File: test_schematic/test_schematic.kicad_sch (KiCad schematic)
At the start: 0 parts

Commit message: Put random components
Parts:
- added C1: C, symbol Device:C
- added R1: R, symbol Device:R
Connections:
- new net: C1.2, R1.1
- new net GND: R1.2

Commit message: Test Push
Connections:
- net GND is gone; now on net +3.3V: R1.2
- net +3.3V: now also C1.1, C1.2, R1.1
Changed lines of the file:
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@@
 	(paper "A4")
+	(junction
+		(at 147.32 97.79)
+		(diameter 0)
+		(color 0 0 0 0)
+	)
+	(junction
+		(at 147.32 93.98)
+		(diameter 0)
+		(color 0 0 0 0)
+	)
 	(junction
 		(at 147.32 100.33)
 		(diameter 0)
 		(color 0 0 0 0)
+	)
+	(junction
+		(at 165.1 86.36)
+		(diameter 0)
+		(color 0 0 0 0)
+	)
+	(junction
+		(at 165.1 88.9)
+		(diameter 0)
+		(color 0 0 0 0)
+	)
+	(wire
+		(pts
+			(xy 147.32 97.79) (xy 138.43 97.79)
+		)
+		(stroke
+			(width 0)
+			(type default)
+		)
 	)
 	(wire
@@
 	(wire
 		(pts
-			(xy 147.32 86.36) (xy 147.32 87.63)
+			(xy 168.91 88.9) (xy 165.1 88.9)
+		)
+		(stroke
+			(width 0)
+			(type default)
+		)
+	)
+	(wire
+		(pts
+			(xy 147.32 86.36) (xy 147.32 93.98)
+		)
+		(stroke
+			(width 0)
+			(type default)
+		)
+	)
+	(wire
+		(pts
+			(xy 165.1 88.9) (xy 165.1 90.17)
 		)
 		(stroke
@@
 		(pts
 			(xy 165.1 97.79) (xy 165.1 100.33)
+		)
+		(stroke
+			(width 0)
+			(type default)
+		)
+	)
+	(wire
+		(pts
+			(xy 165.1 86.36) (xy 167.64 86.36)
+		)
+		(stroke
+			(width 0)
+			(type default)
+		)
+	)
+	(wire
+		(pts
+			(xy 144.78 87.63) (xy 144.78 93.98)
+		)
+		(stroke
+			(width 0)
+			(type default)
+		)
+	)
+	(wire
+		(pts
+			(xy 147.32 93.98) (xy 147.32 97.79)
 		)
 		(stroke
@@
 	(wire
 		(pts
-			(xy 165.1 86.36) (xy 165.1 90.17)
+			(xy 165.1 86.36) (xy 165.1 88.9)
 		)
 		(stroke
+			(width 0)
+			(type default)
+		)
+	)
+	(wire
+		(pts
+			(xy 167.64 83.82) (xy 167.64 86.36)
+		)
+		(stroke
+			(width 0)
+			(type default)
+		)
+	)
+	(wire
+		(pts
+			(xy 168.91 83.82) (xy 168.91 88.9)
+		)
+		(stroke
+			(width 0)
+			(type default)
+		)
+	)
+	(wire
+		(pts
+			(xy 144.78 93.98) (xy 147.32 93.98)
+		)
+		(stroke

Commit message: Pushing my Changes
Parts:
- added D1: 1N62xxA, Diode_THT:D_DO-201AE_P15.24mm_Horizontal, symbol Diode:1N62xxA
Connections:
- net +3.3V: now also D1.1 (A1), D1.2 (A2)
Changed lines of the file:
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@@
 	(paper "A4")
+	(junction
+		(at 151.13 100.33)
+		(diameter 0)
+		(color 0 0 0 0)
+	)
 	(junction
 		(at 147.32 97.79)
@@
 	)
 	(junction
+		(at 161.29 100.33)
+		(diameter 0)
+		(color 0 0 0 0)
+	)
+	(junction
 		(at 165.1 86.36)
 		(diameter 0)
@@
 	(wire
 		(pts
+			(xy 151.13 95.25) (xy 151.13 100.33)
+		)
+		(stroke
+			(width 0)
+			(type default)
+		)
+	)
+	(wire
+		(pts
 			(xy 158.75 86.36) (xy 165.1 86.36)
 		)
@@
 	(wire
 		(pts
+			(xy 161.29 95.25) (xy 161.29 100.33)
+		)
+		(stroke
+			(width 0)
+			(type default)
+		)
+	)
+	(wire
+		(pts
 			(xy 147.32 86.36) (xy 147.32 93.98)
 		)
@@
 	(wire
 		(pts
-			(xy 147.32 100.33) (xy 165.1 100.33)
+			(xy 147.32 100.33) (xy 151.13 100.33)
+		)
+		(stroke
+			(width 0)
+			(type default)
+		)
+	)
+	(wire
+		(pts
+			(xy 158.75 95.25) (xy 161.29 95.25)
+		)
+		(stroke
+			(width 0)
+			(type default)
+		)
+	)
+	(wire
+		(pts
+			(xy 161.29 100.33) (xy 165.1 100.33)
 		)
 		(stroke
@@
 		(pts
 			(xy 144.78 93.98) (xy 147.32 93.98)
+		)
+		(stroke
+			(width 0)
+			(type default)
+		)
+	)
+	(wire
+		(pts
+			(xy 151.13 100.33) (xy 161.29 100.33)
 		)
 		(stroke
@@
 					(unit 1)
 				)
+			)
+		)
+	)
+	(symbol
+		(lib_id "Diode:1N62xxA")
+		(at 154.94 95.25 0)
+		(unit 1)
+		(exclude_from_sim no)
+		(in_bom yes)
+		(on_board yes)
+		(dnp no)
+		(fields_autoplaced yes)
+		(property "Reference" "D1"
+			(at 154.94 88.9 0)
+			(effects
+				(font
+					(size 1.27 1.27)
+				)
+			)
+		)
+		(property "Value" "1N62xxA"
+			(at 154.94 91.44 0)
+			(effects
+				(font
+					(size 1.27 1.27)
+				)
+			)
+		)
+		(property "Footprint" "Diode_THT:D_DO-201AE_P15.24mm_Horizontal"
+			(at 154.94 100.33 0)
+			(effects
+				(font
+					(size 1.27 1.27)
+				)
+				(hide yes)
+			)
+		)
+		(property "Datasheet" "https://www.vishay.com/docs/88301/15ke.pdf"
+			(at 153.67 95.25 0)
+			(effects
+				(font
+					(size 1.27 1.27)
+				)
+				(hide yes)
+			)
+		)
+		(property "Description" "1500W unidirectional TRANSZORB® Transient Voltage Suppressor, DO-201AE"
+			(at 154.94 95.25 0)
+			(effects
+				(font
+					(size 1.27 1.27)
+				)
+				(hide yes)
+			)
+		)
+		(pin "1"
+		)
+		(pin "2"
+		)
+		(instances
+			(project ""
+				(path "/34cad894-6d1f-473e-a83f-d88de5da818d"
+					(reference "D1")
+					(unit 1)
+				)

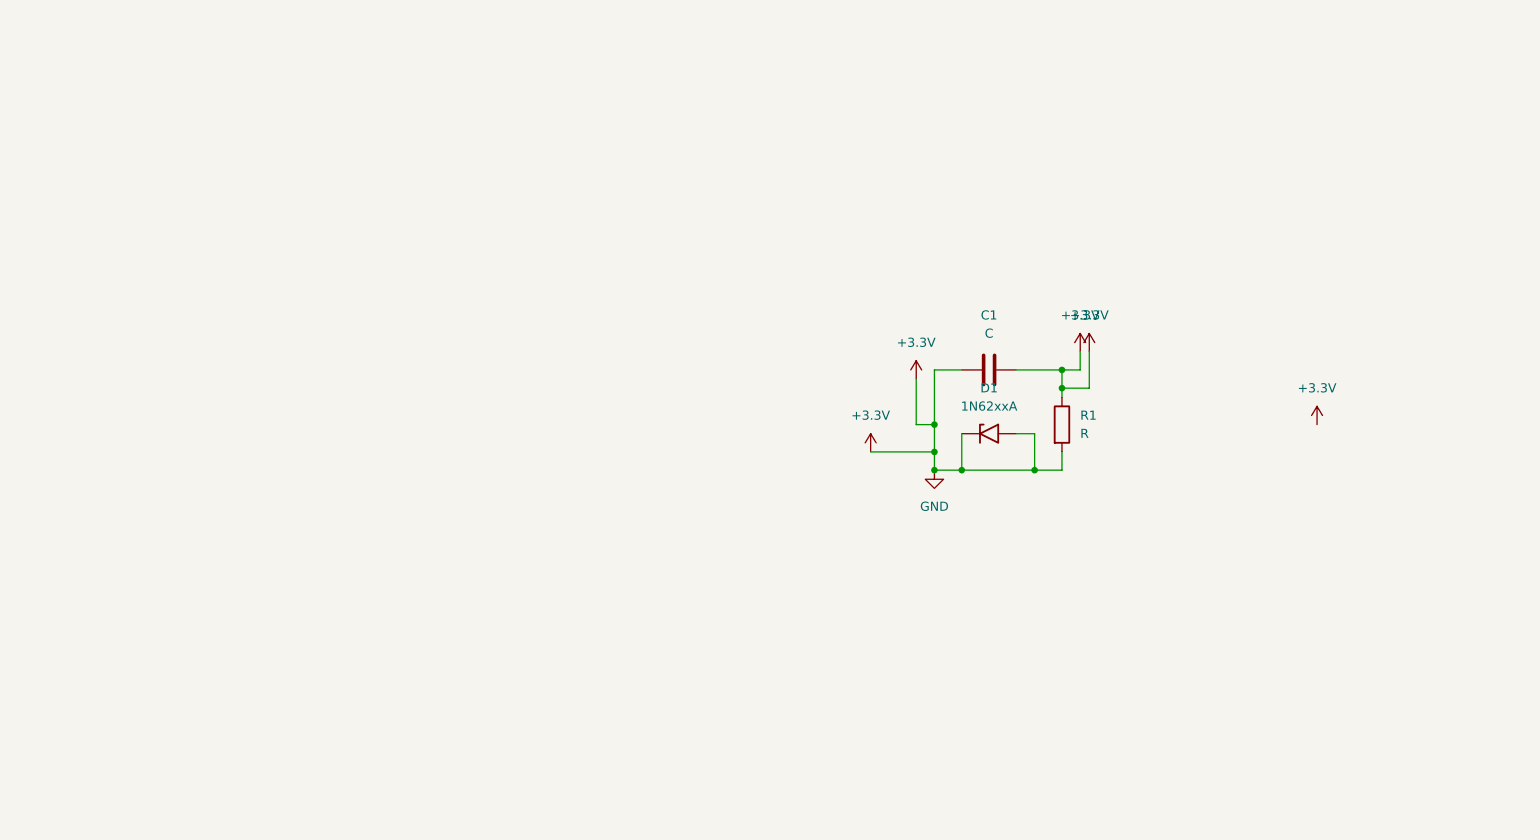
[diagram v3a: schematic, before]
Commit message: Started wiring up digipots
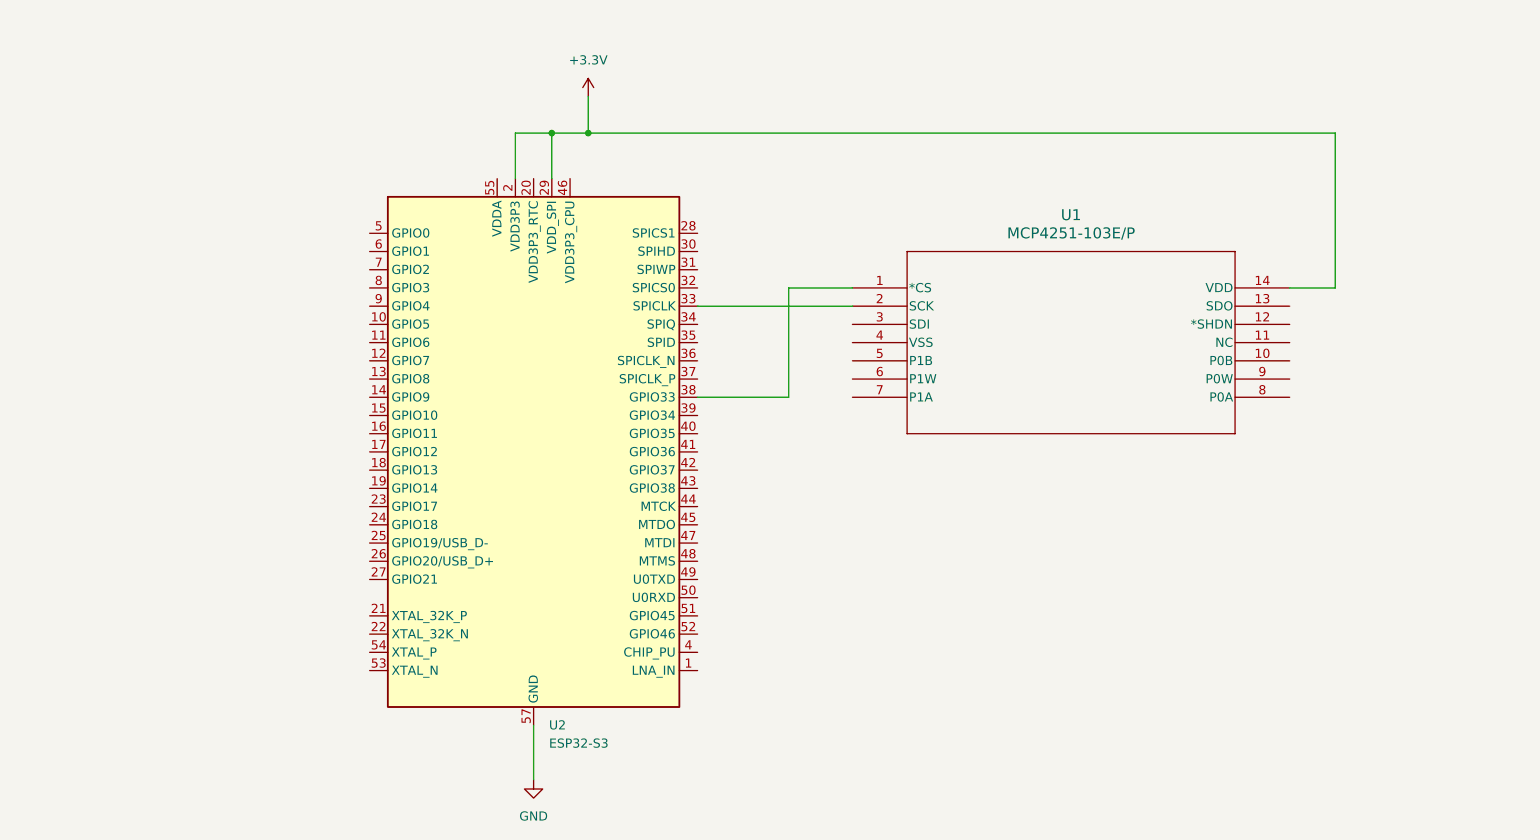
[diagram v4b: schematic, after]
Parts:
- removed C1: C, symbol Device:C
- removed D1: 1N62xxA, Diode_THT:D_DO-201AE_P15.24mm_Horizontal, symbol Diode:1N62xxA
- removed R1: R, symbol Device:R
- added U1: MCP4251-103E/P, PDIP14_300MC_MCH, symbol 2026-03-31_23-59-55:MCP4251-103E_P
- added U2: ESP32-S3, Package_DFN_QFN:QFN-56-1EP_7x7mm_P0.4mm_EP4x4mm, symbol MCU_Espressif:ESP32-S3
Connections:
- net +3.3V: now also U1.14 (VDD), U2.2 (VDD3P3), U2.29 (VDD_SPI), U2.3 (VDD3P3)
- new net: U1.2 (SCK), U2.33 (SPICLK)
- new net: U1.1 (*CS), U2.38 (GPIO33)
- new net: U2.55 (VDDA), U2.56 (VDDA)
- new net GND: U2.57 (GND)

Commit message: Pushing updates
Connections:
- net at U2.34 (SPIQ): now also U1.13 (SDO)
- net at U2.35 (SPID): now also U1.3 (SDI)
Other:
- note added: "Digipot (Left Joystick)"
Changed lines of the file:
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@@
 	(generator_version "9.0")
 	(paper "A4")
+	(text "Digipot (Left Joystick)"
+		(exclude_from_sim no)
+		(at 166.37 82.55 0)
+		(effects
+			(font
+				(size 1.27 1.27)
+			)
+		)
+	)
 	(junction
 		(at 99.06 53.34)
@@
 		(diameter 0)
 		(color 0 0 0 0)
+	)
+	(wire
+		(pts
+			(xy 135.89 80.01) (xy 132.08 80.01)
+		)
+		(stroke
+			(width 0)
+			(type default)
+		)
 	)
 	(wire
@@
 	(wire
 		(pts
+			(xy 132.08 80.01) (xy 132.08 82.55)
+		)
+		(stroke
+			(width 0)
+			(type default)
+		)
+	)
+	(wire
+		(pts
 			(xy 99.06 48.26) (xy 99.06 53.34)
+		)
+		(stroke
+			(width 0)
+			(type default)
+		)
+	)
+	(wire
+		(pts
+			(xy 204.47 100.33) (xy 129.54 100.33)
 		)
 		(stroke
@@
 	(wire
 		(pts
+			(xy 204.47 77.47) (xy 204.47 100.33)
+		)
+		(stroke
+			(width 0)
+			(type default)
+		)
+	)
+	(wire
+		(pts
+			(xy 196.85 77.47) (xy 204.47 77.47)
+		)
+		(stroke
+			(width 0)
+			(type default)
+		)
+	)
+	(wire
+		(pts
+			(xy 132.08 82.55) (xy 114.3 82.55)
+		)
+		(stroke
+			(width 0)
+			(type default)
+		)
+	)
+	(wire
+		(pts
 			(xy 88.9 53.34) (xy 88.9 59.69)
+		)
+		(stroke
+			(width 0)
+			(type default)
+		)
+	)
+	(wire
+		(pts
+			(xy 129.54 100.33) (xy 129.54 80.01)
 		)
 		(stroke
@@
 		)
 		(stroke
+			(width 0)
+			(type default)
+		)
+	)
+	(wire
+		(pts
+			(xy 129.54 80.01) (xy 114.3 80.01)
+		)
+		(stroke

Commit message: Update test_schematic.kicad_sch
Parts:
- added SW1, SW2: SW_Push, symbol Switch:SW_Push
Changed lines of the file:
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@@
+	)
+	(symbol
+		(lib_id "Switch:SW_Push")
+		(at 46.99 74.93 0)
+		(unit 1)
+		(exclude_from_sim no)
+		(in_bom yes)
+		(on_board yes)
+		(dnp no)
+		(fields_autoplaced yes)
+		(property "Reference" "SW1"
+			(at 46.99 67.31 0)
+			(effects
+				(font
+					(size 1.27 1.27)
+				)
+			)
+		)
+		(property "Value" "SW_Push"
+			(at 46.99 69.85 0)
+			(effects
+				(font
+					(size 1.27 1.27)
+				)
+			)
+		)
+		(property "Footprint" ""
+			(at 46.99 69.85 0)
+			(effects
+				(font
+					(size 1.27 1.27)
+				)
+				(hide yes)
+			)
+		)
+		(property "Datasheet" "~"
+			(at 46.99 69.85 0)
+			(effects
+				(font
+					(size 1.27 1.27)
+				)
+				(hide yes)
+			)
+		)
+		(property "Description" "Push button switch, generic, two pins"
+			(at 46.99 74.93 0)
+			(effects
+				(font
+					(size 1.27 1.27)
+				)
+				(hide yes)
+			)
+		)
+		(pin "1"
+		)
+		(pin "2"
+		)
+		(instances
+			(project ""
+				(path "/34cad894-6d1f-473e-a83f-d88de5da818d"
+					(reference "SW1")
+					(unit 1)
+				)
+			)
+		)
 	)
 	(symbol
@@
 					(unit 1)
 				)
+			)
+		)
+	)
+	(symbol
+		(lib_id "Switch:SW_Push")
+		(at 46.99 90.17 0)
+		(unit 1)
+		(exclude_from_sim no)
+		(in_bom yes)
+		(on_board yes)
+		(dnp no)
+		(fields_autoplaced yes)
+		(property "Reference" "SW2"
+			(at 46.99 82.55 0)
+			(effects
+				(font
+					(size 1.27 1.27)
+				)
+			)
+		)
+		(property "Value" "SW_Push"
+			(at 46.99 85.09 0)
+			(effects
+				(font
+					(size 1.27 1.27)
+				)
+			)
+		)
+		(property "Footprint" ""
+			(at 46.99 85.09 0)
+			(effects
+				(font
+					(size 1.27 1.27)
+				)
+				(hide yes)
+			)
+		)
+		(property "Datasheet" "~"
+			(at 46.99 85.09 0)
+			(effects
+				(font
+					(size 1.27 1.27)
+				)
+				(hide yes)
+			)
+		)
+		(property "Description" "Push button switch, generic, two pins"
+			(at 46.99 90.17 0)
+			(effects
+				(font
+					(size 1.27 1.27)
+				)
+				(hide yes)
+			)
+		)
+		(pin "1"
+		)
+		(pin "2"
+		)
+		(instances
+			(project "test_schematic"
+				(path "/34cad894-6d1f-473e-a83f-d88de5da818d"
+					(reference "SW2")
+					(unit 1)
+				)

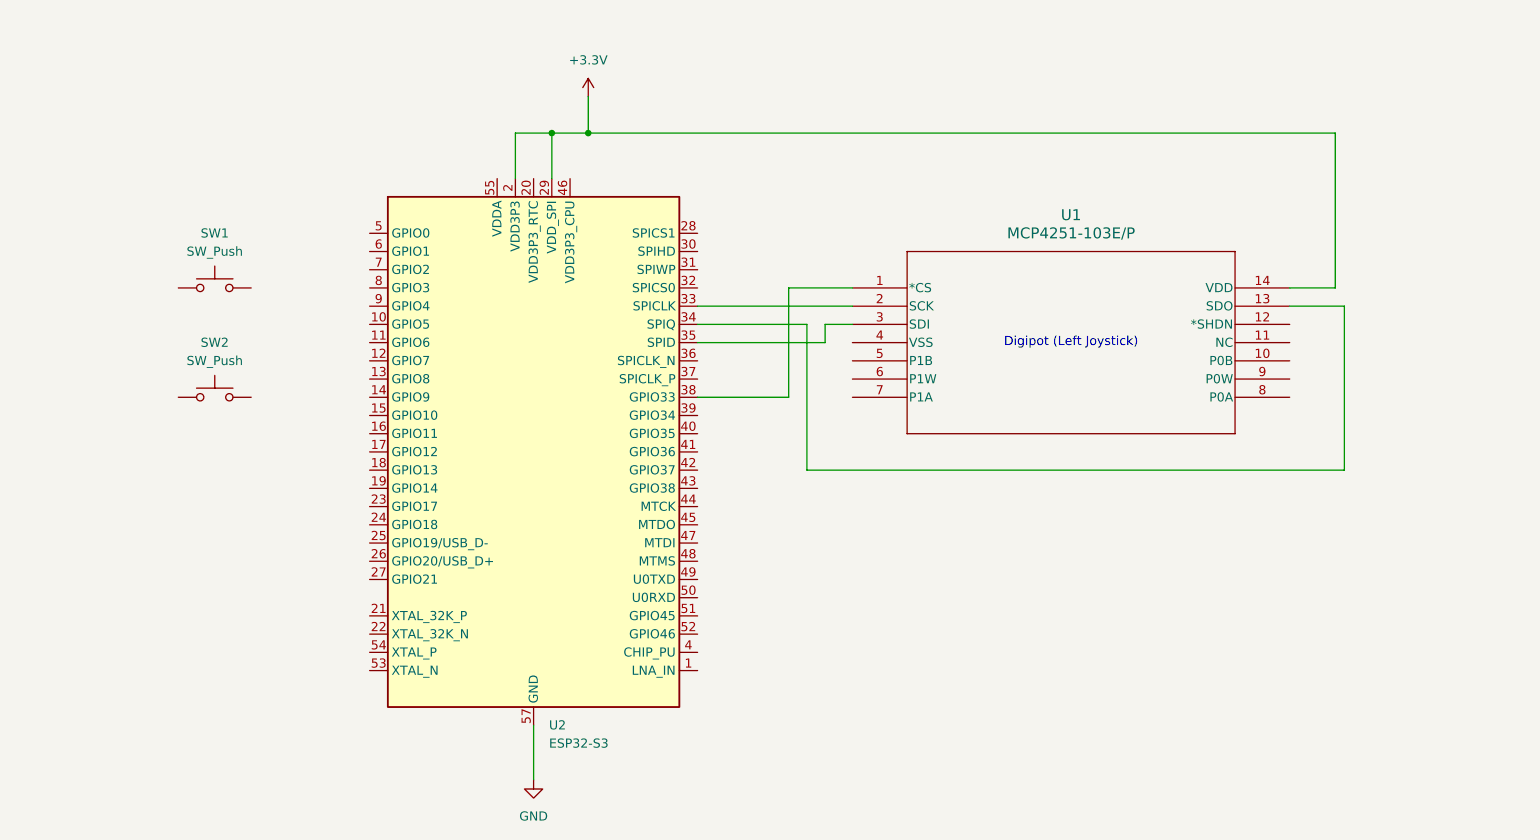
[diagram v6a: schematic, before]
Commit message: Everything BUT the IMU and switches
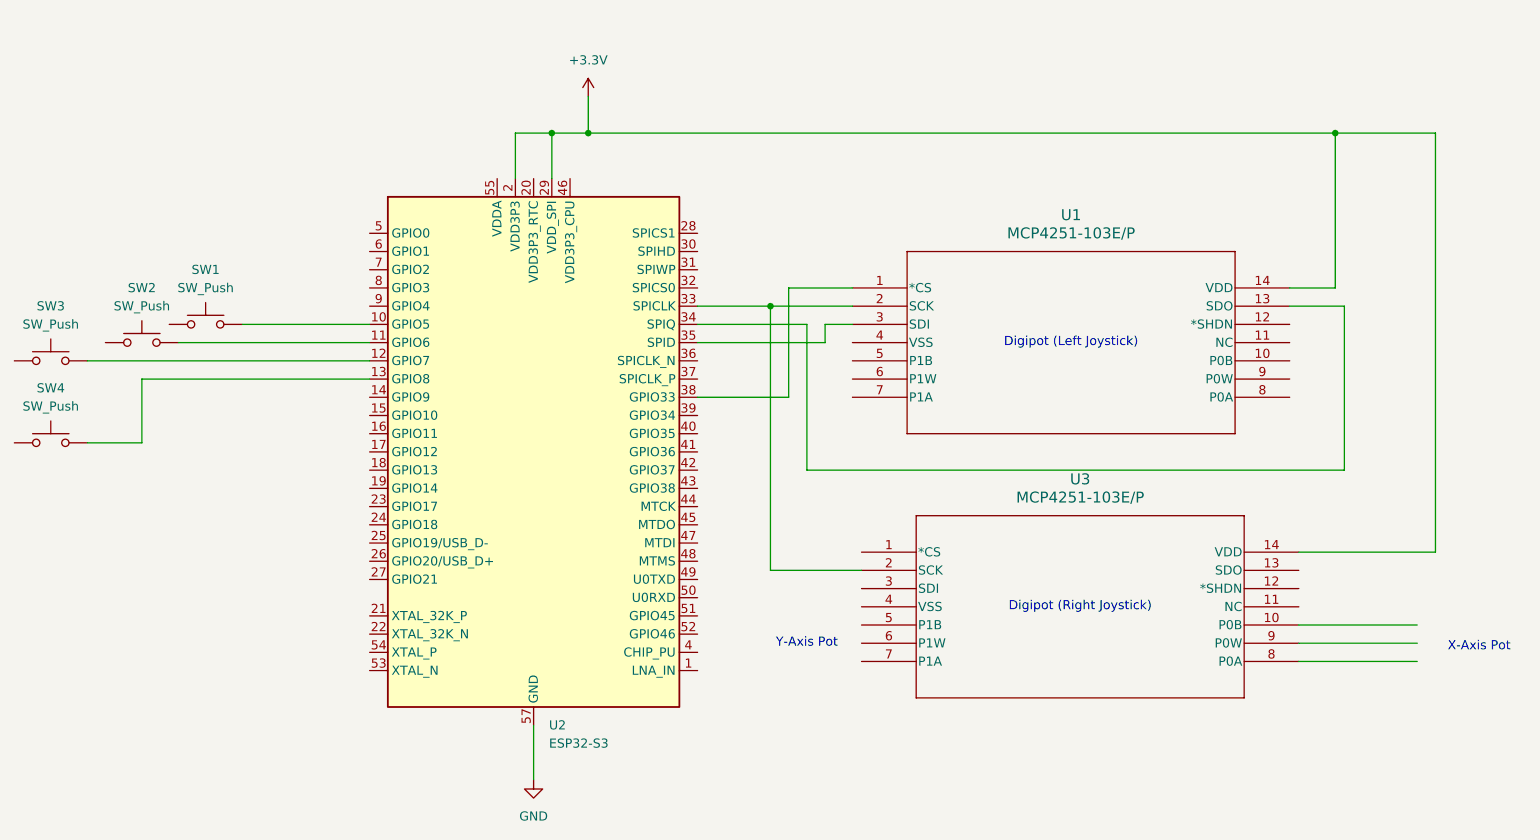
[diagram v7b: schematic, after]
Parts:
- added SW3, SW4: SW_Push, symbol Switch:SW_Push
- added U3: MCP4251-103E/P, PDIP14_300MC_MCH, symbol 2026-03-31_23-59-55:MCP4251-103E_P
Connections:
- net +3.3V: now also U3.14 (VDD)
- net at SW1.2: now also U2.10 (GPIO5)
- net at SW2.2: now also U2.11 (GPIO6)
- net at U2.12 (GPIO7): now also SW3.2
- net at U2.13 (GPIO8): now also SW4.2
- net at U1.2 (SCK), U2.33 (SPICLK): now also U3.2 (SCK)
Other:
- note added: "Digipot (Right Joystick)"
- note added: "X-Axis Pot"
- note added: "Y-Axis Pot"
- moved on the sheet: SW1

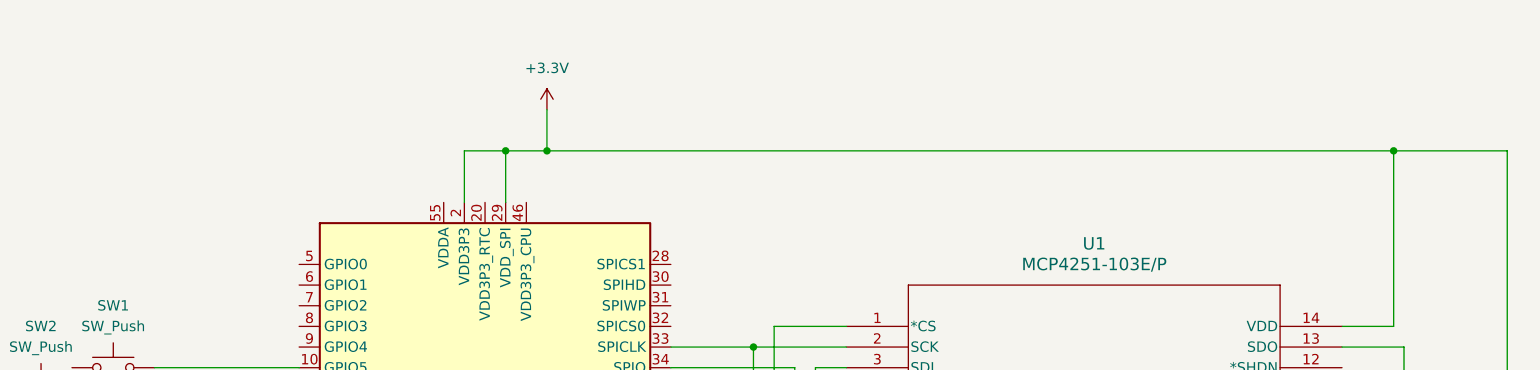
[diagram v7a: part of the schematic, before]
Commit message: Added some decoupling capacitors for power supply
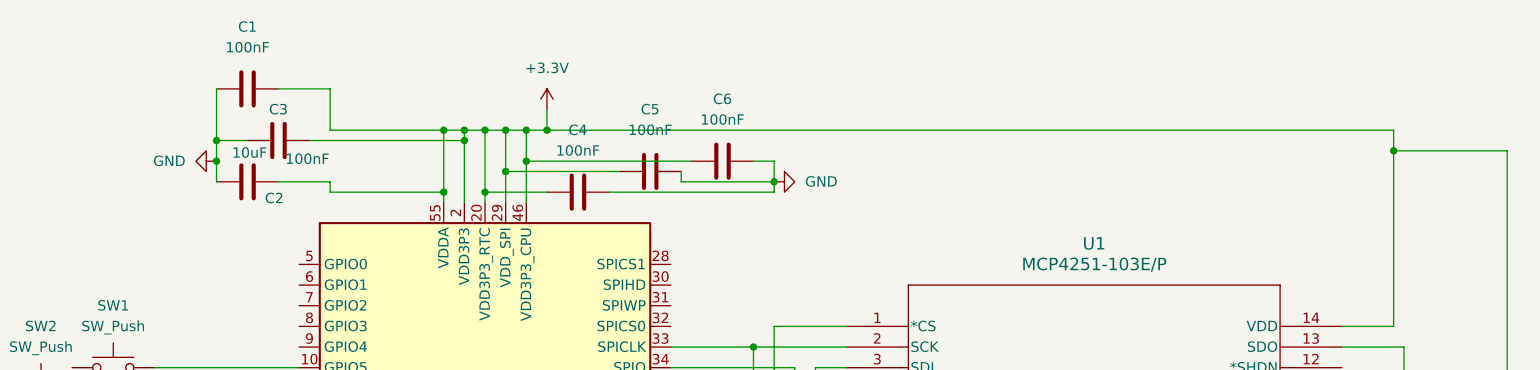
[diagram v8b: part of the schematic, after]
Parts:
- added C1, C3, C4, C5, C6: 100nF, symbol Device:C
- added C2: 10uF, symbol Device:C
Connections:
- net +3.3V: now also U2.20 (VDD3P3_RTC), U2.46 (VDD3P3_CPU), U2.55 (VDDA), U2.56 (VDDA), C1.1, C2.1, C3.1, C4.2, C5.2, C6.2
- net GND: now also C1.2, C2.2, C3.2, C4.1, C5.1, C6.1
